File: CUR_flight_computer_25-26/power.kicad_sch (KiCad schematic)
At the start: 20 parts, among them J2 TB0011-350-02GR, J3 TB0011-350-02GR, J4 XT30U-M, J5 XT30U-M, U15 ZXCT180B4W5, U16 ZXCT180B4W5, U7 LM66200, U8 NCP186AMX330TAG

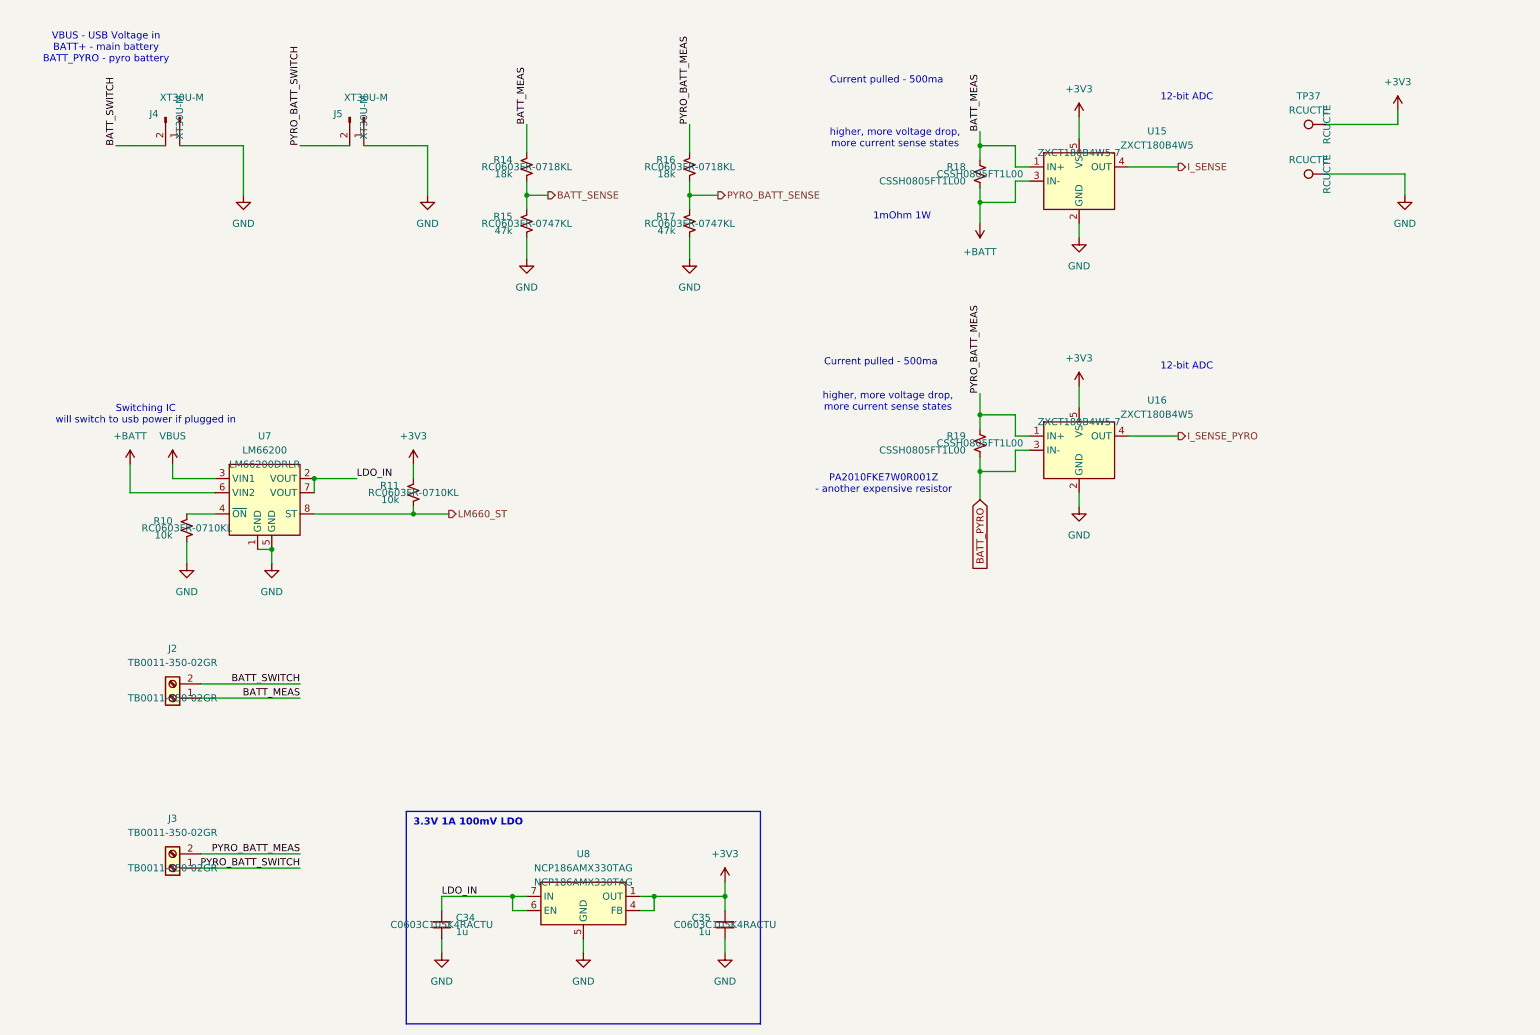
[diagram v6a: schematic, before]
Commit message: Hide MPNs
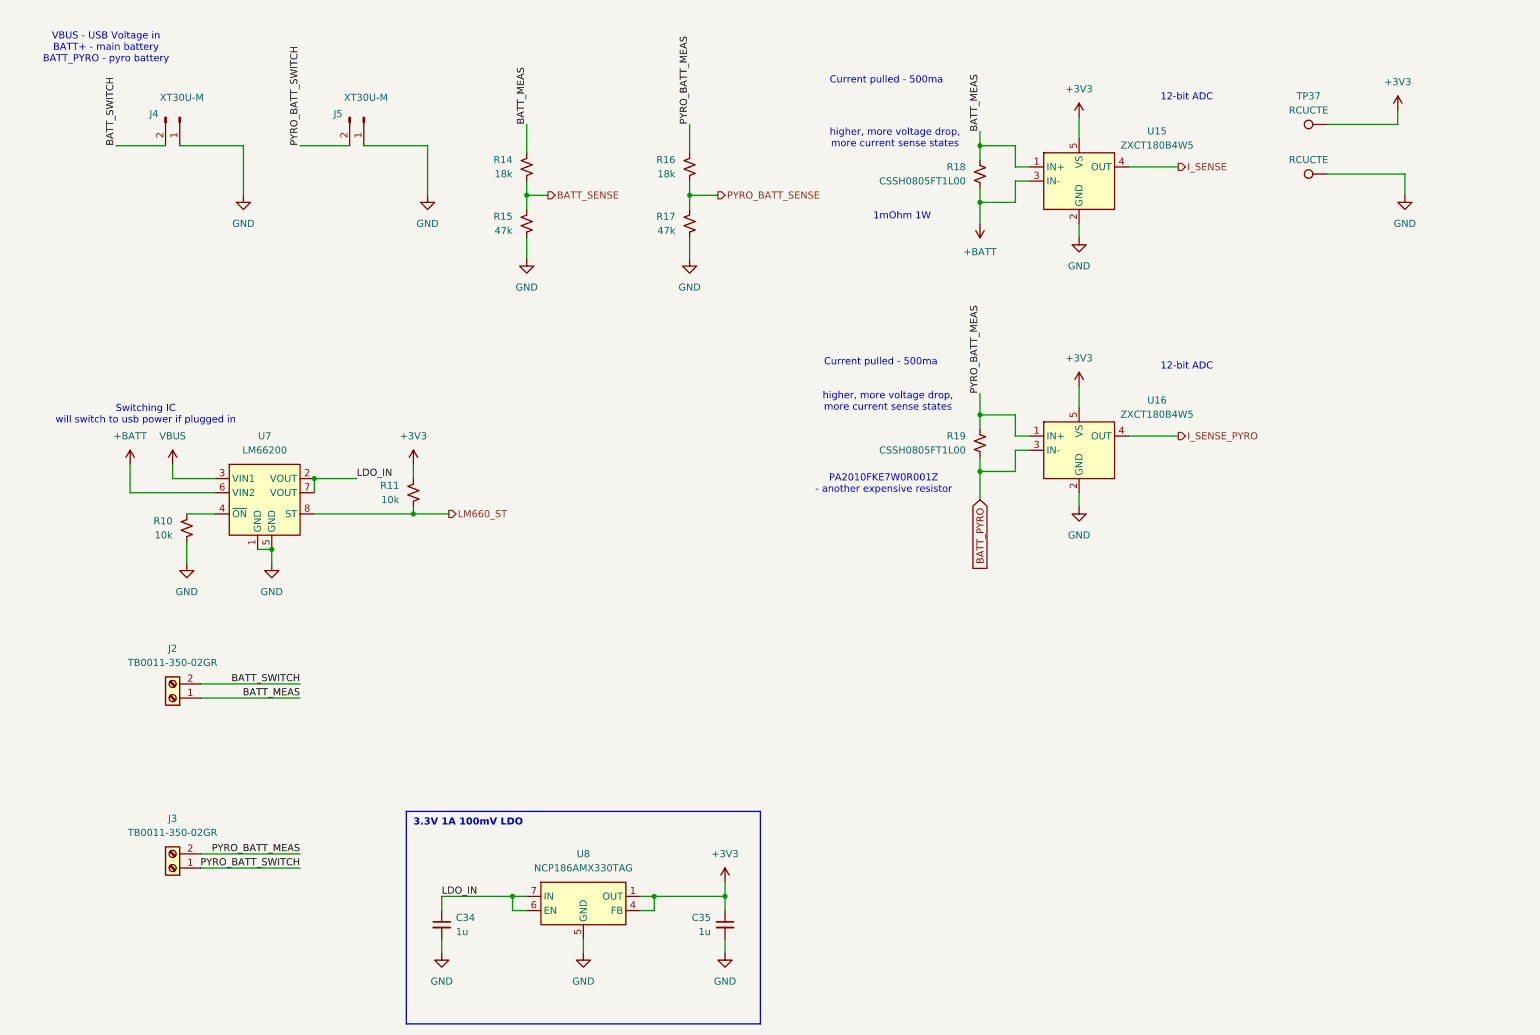
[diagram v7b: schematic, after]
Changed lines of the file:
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@@
 					(size 1.27 1.27)
 				)
+				(hide yes)
 			)
 		)
@@
 					(size 1.27 1.27)
 				)
+				(hide yes)
 			)
 		)
@@
 					(size 1.27 1.27)
 				)
+				(hide yes)
 			)
 		)
@@
 					(size 1.27 1.27)
 				)
+				(hide yes)
 			)
 		)
@@
 					(size 1.27 1.27)
 				)
+				(hide yes)
 			)
 		)
@@
 					(size 1.27 1.27)
 				)
+				(hide yes)
 			)
 		)
@@
 					(size 1.27 1.27)
 				)
+				(hide yes)
 			)
 		)
@@
 					(size 1.27 1.27)
 				)
+				(hide yes)
 			)
 		)
@@
 					(size 1.27 1.27)
 				)
+				(hide yes)
 			)
 		)
@@
 					(size 1.27 1.27)
 				)
+				(hide yes)
 			)
 		)
@@
 					(size 1.27 1.27)
 				)
+				(hide yes)
 			)
 		)
@@
 					(size 1.27 1.27)
 				)
+				(hide yes)
 			)
 		)
@@
 					(size 1.27 1.27)
 				)
+				(hide yes)
 			)
 		)
@@
 					(size 1.27 1.27)
 				)
+				(hide yes)
 			)
 		)
@@
 					(size 1.27 1.27)
 				)
+				(hide yes)
 			)
 		)
@@
 					(size 1.27 1.27)
 				)
+				(hide yes)
 			)
 		)
@@
 					(size 1.27 1.27)
 				)
+				(hide yes)
 			)
 		)
@@
 					(size 1.27 1.27)
 				)
+				(hide yes)
 			)
 		)
@@
 					(size 1.27 1.27)
 				)
+				(hide yes)
 			)
 		)
@@
 					(size 1.27 1.27)
 				)
-			)
-		)
+				(hide yes)
+			)
+		)

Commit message: Cleaned up schematic
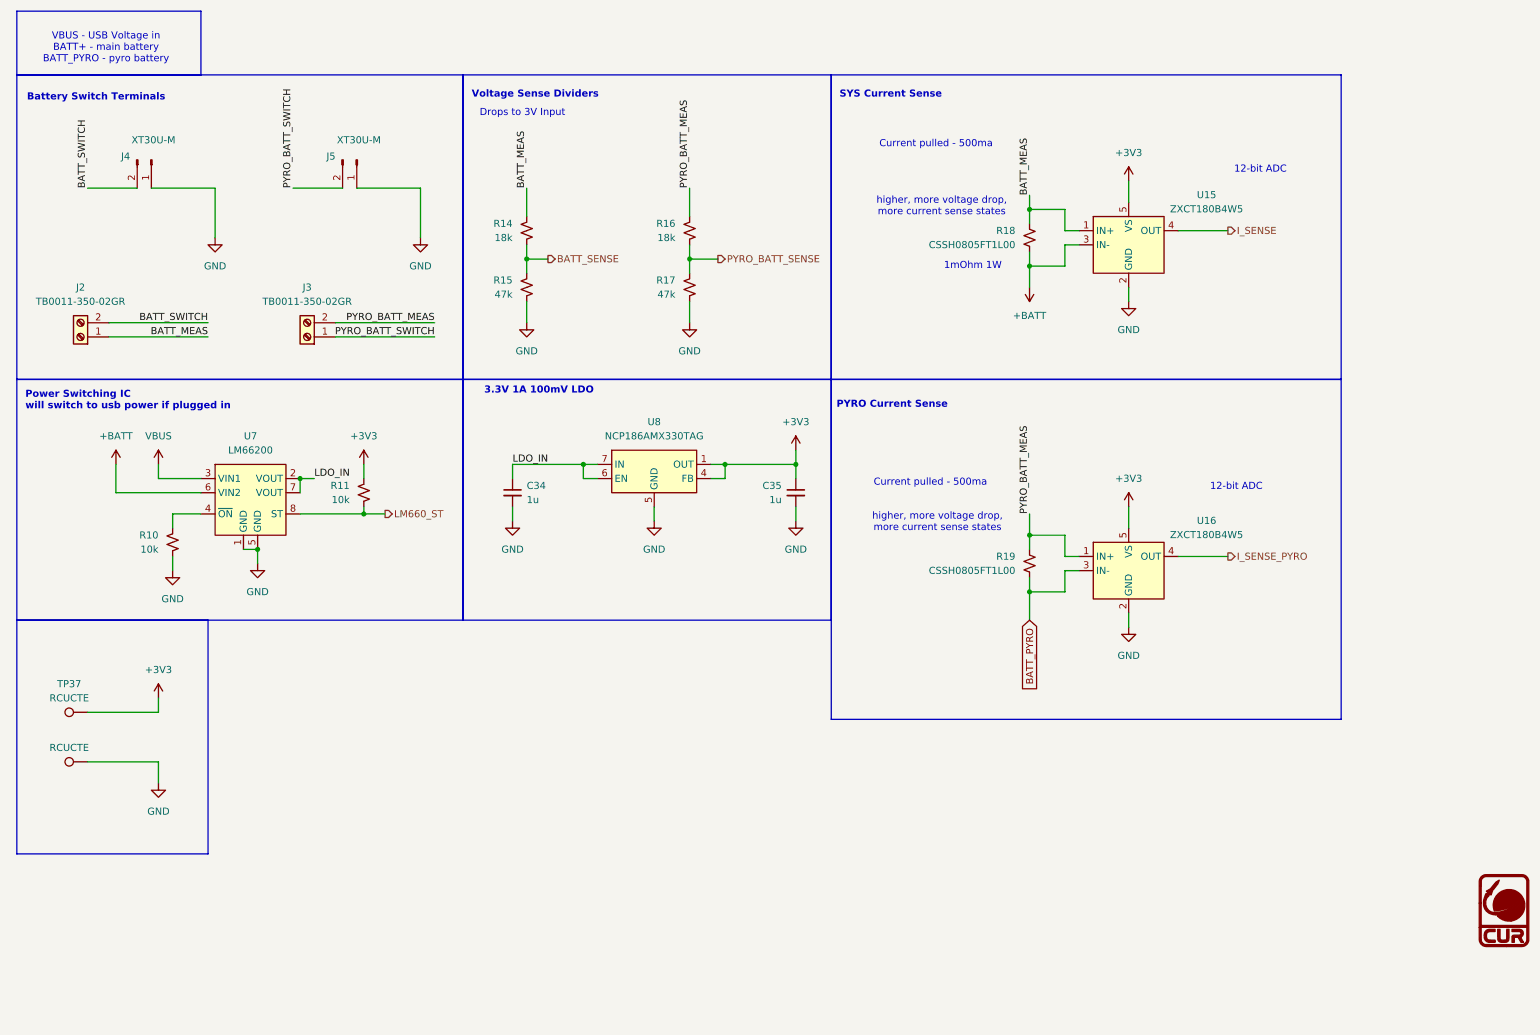
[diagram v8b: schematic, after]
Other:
- note added: "Battery Switch Terminals"
- note added: "Drops to 3V Input"
- note added: "PYRO Current Sense"
- note added: "Power Switching IC will switch to usb power if plugged in"
- note added: "SYS Current Sense"
- note added: "Voltage Sense Dividers"
- note removed: "PA2010FKE7W0R001Z - another expensive resistor"
- note removed: "Switching IC will switch to usb power if plugged in"
- company: (none) -> Clarkson University Rocketry
- title: (none) -> Flight Computer
- moved on the sheet: C34, C35, J2, J3, J4, J5, R10, R11, R14, R15, R16, R17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
